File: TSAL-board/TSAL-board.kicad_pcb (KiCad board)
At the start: 2 copper layers, 82.5 x 65 mm, 75 parts, among them J1 BM02B-PASS-1-TF, J2 19427-0040, J3 BM02B-PASS-1-TF, J4 BM02B-PASS-1-TF, Q1 DMP3098LQ-7, Q2 2N7002K-AU, Q3 2N7002K-AU, Q4 2N7002K-AU, U1 TL431QDBVR, U2 TLP291(GB,SE, U3 TLC555QDRQ1

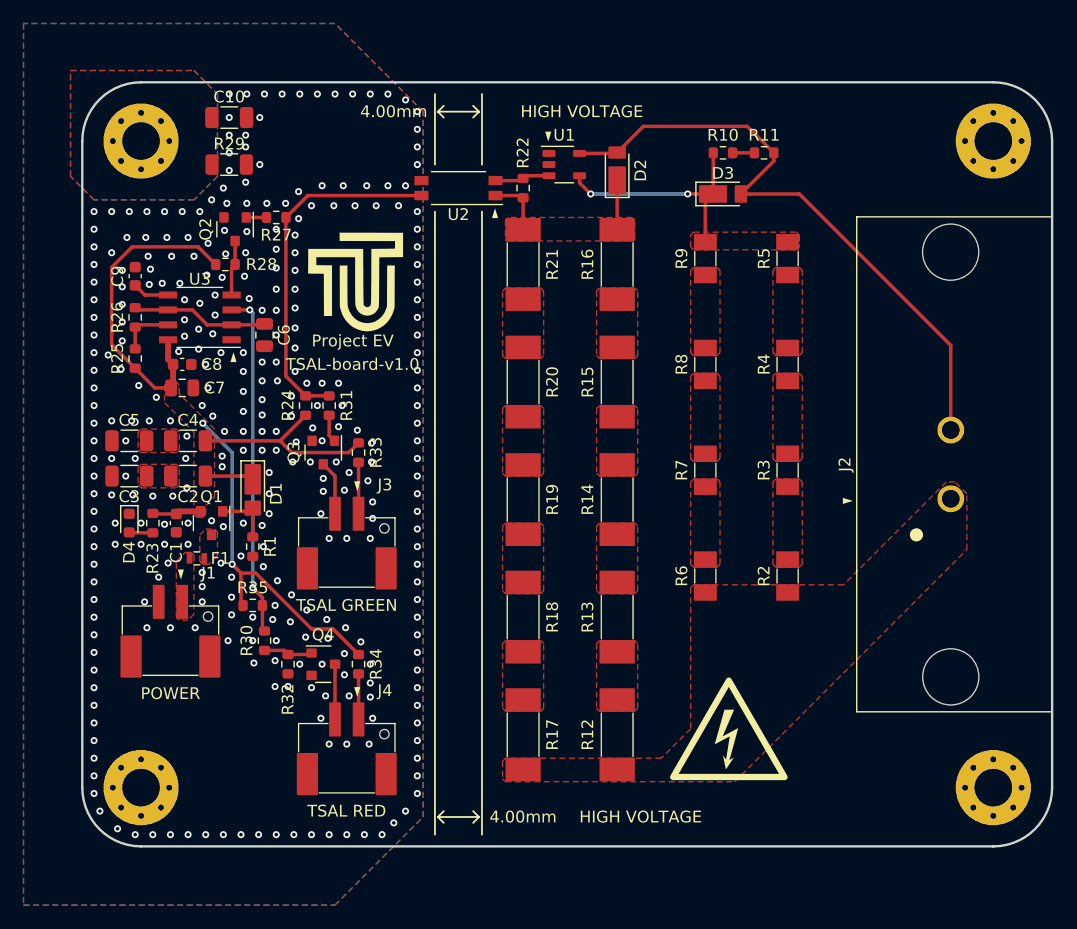
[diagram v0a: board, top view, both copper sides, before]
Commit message: 補償回路、シュミットトリガ回路追加
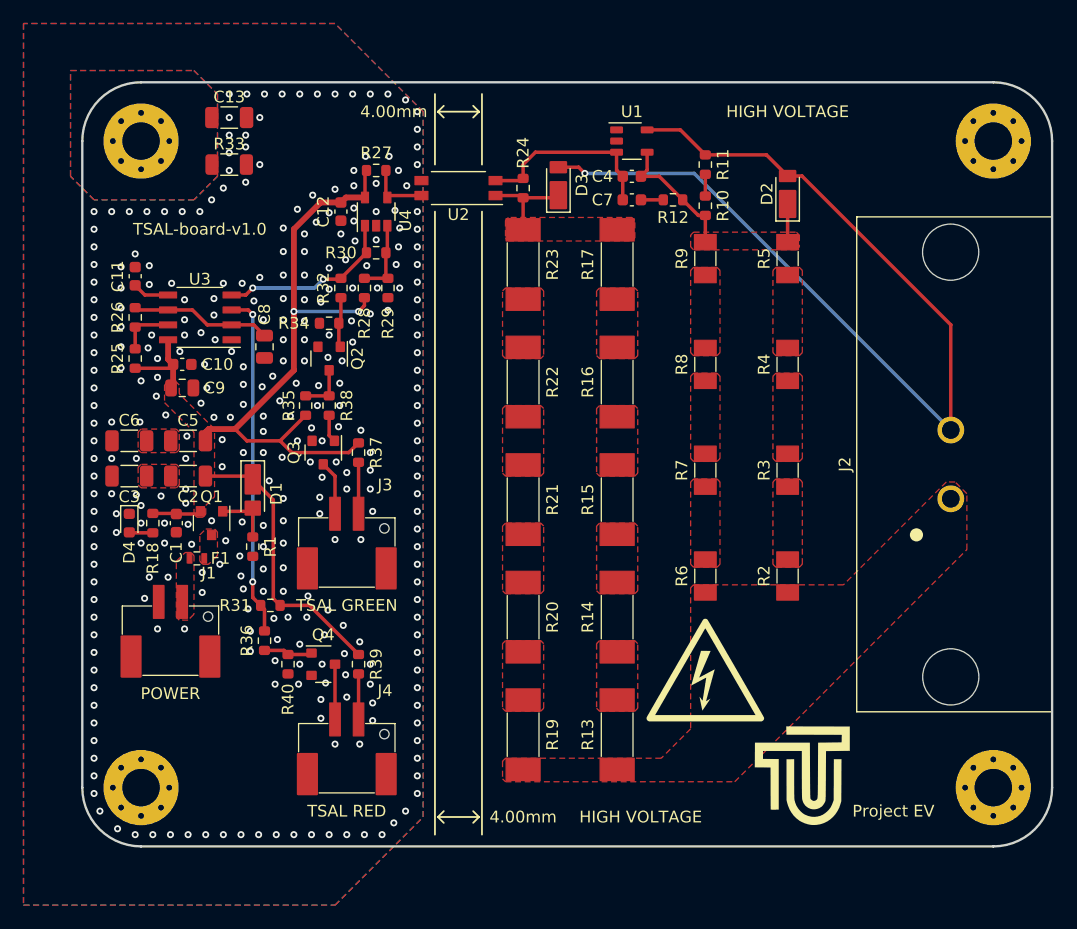
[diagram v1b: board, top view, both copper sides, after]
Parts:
- removed the R27 at (16.5, 11.5)
- removed REF** (x7): Identifier_1pin, ProjectEV:Identifier_1pin
- added C12: 0.1u, Capacitor_SMD:C_0603_1608Metric, F.Cu at (22.0, 11.0)
- added C4: 100p, Capacitor_SMD:C_0603_1608Metric, F.Cu at (46.8, 8.00)
- added C7: 10n, Capacitor_SMD:C_0603_1608Metric, F.Cu at (46.8, 10.0)
- added R12: 10k, Resistor_SMD:R_0603_1608Metric, F.Cu at (50.2, 10.0)
- added R29: 100k, Resistor_SMD:R_0603_1608Metric, F.Cu at (26.0, 17.5)
- added R30: 51k, Resistor_SMD:R_0603_1608Metric, F.Cu at (25.0, 14.5)
- added R32: 100, Resistor_SMD:R_0603_1608Metric, F.Cu at (22.0, 17.5)
- added R34: 1M, Resistor_SMD:R_0603_1608Metric, F.Cu at (21.0, 20.5)
- added R35: 100k, Resistor_SMD:R_0603_1608Metric, F.Cu at (19.0, 27.5)
- added U4: NCV20071SN2T1G, ProjectEV:Package_SOT-23-5_NCV20071SN2T1G, F.Cu at (25.0, 11.0)
- R11: value 3.9k -> 4.3k
- R27: renamed from R24; value 1M -> 10k
- moved G*** 56.6 mm to (61.0, 59.0)
- moved R27 20.9 mm to (25.0, 7.50), turned to 0 degrees
- moved Q2 13.6 mm to (21.0, 23.5)
- moved R28 12.0 mm to (24.0, 17.5), turned to 90 degrees
- moved U1 6.09 mm to (46.8, 5.00)
- moved D2 5.50 mm to (60.0, 9.50), turned to 90 degrees
- moved G*** 5.39 mm to (53.0, 50.0)
- moved D3 5.15 mm to (40.5, 8.75)
- moved R11 5.10 mm to (53.0, 7.00), turned to 90 degrees
- moved R10 4.74 mm to (53.0, 10.5), turned to 90 degrees
- moved R31 1.50 mm to (16.0, 44.5), turned to 180 degrees
- moved C8 1.00 mm to (15.5, 22.5)
- renumbered C8 to C10, C9 to C11, C10 to C13, C4 to C5, C5 to C6, C6 to C8, C7 to C9, D3 to D2, D2 to D3, R12 to R13, R13 to R14, R14 to R15, R15 to R16, R16 to R17, R23 to R18, R17 to R19, R18 to R20, R19 to R21, R20 to R22, R21 to R23, R22 to R24, R35 to R31, R29 to R33, R30 to R36, R33 to R37, R31 to R38, R34 to R39, R32 to R40
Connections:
- net Net-(C10-Pad1) renamed Earth
- Q2 pad 3: /~{RST} -> Net-(Q2-D)
- R28 pad 2: /~{RST} -> Net-(U4-+)
- R38 pad 1: /~{TS_ACTIVE} -> Net-(Q2-D)
- U3 pad 4: /~{RST} -> /TS_ACTIVE
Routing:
- net /TS-: track 53.5 -> 84.3 mm, vias 0 -> 1
- net /~{TS_ACTIVE}: track 30.2 -> 5.32 mm
- net /TS_ACTIVE: track 0.00 -> 15.3 mm, vias 0 -> 2
- net Net-(U1-K): track 4.72 -> 16.3 mm
- net +12V: track 82.6 -> 89.7 mm
- net Net-(U4-+): track 0.00 -> 6.60 mm
- net Net-(D2-K): track 20.2 -> 14.6 mm, vias 2 -> 0
- net /~{RST}: track 4.72 -> 0.00 mm
- net Net-(Q2-D): track 0.00 -> 4.18 mm
- net Net-(Q2-G): track 1.73 -> 4.30 mm
- net Net-(C7-Pad2): track 0.00 -> 1.90 mm
- net Net-(D3-K): track 9.35 -> 8.25 mm
- net GND: vias 322 -> 317

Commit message: 1ピン識別子追加
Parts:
- added REF**: Identifier_1pin, ProjectEV:Identifier_1pin, F.Cu at (8.50, 42.2)
- added REF**: Identifier_1pin, ProjectEV:Identifier_1pin, F.Cu at (35.2, 10.8)
- added REF**: Identifier_1pin, ProjectEV:Identifier_1pin, F.Cu at (44.2, 4.00)
- added REF**: Identifier_1pin, ProjectEV:Identifier_1pin, F.Cu at (23.0, 12.8)
- added REF**: Identifier_1pin, ProjectEV:Identifier_1pin, F.Cu at (13.2, 23.0)
- added REF**: Identifier_1pin, ProjectEV:Identifier_1pin, F.Cu at (23.5, 52.2)
- added REF**: Identifier_1pin, ProjectEV:Identifier_1pin, F.Cu at (65.2, 35.5)
- added REF**: Identifier_1pin, ProjectEV:Identifier_1pin, F.Cu at (23.5, 34.8)
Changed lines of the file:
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@@
     )
   )
+  (footprint "ProjectEV:Identifier_1pin" (layer "F.Cu")
+    (at 8.5 42.25)
+    (attr allow_missing_courtyard)
+    (fp_text reference "REF**" (at 0 -0.5 unlocked) (layer "F.SilkS") hide
+        (effects (font (size 1 1) (thickness 0.1)))
+    )
+    (fp_text value "Identifier_1pin" (at 0 1 unlocked) (layer "F.Fab")
+        (effects (font (size 1 1) (thickness 0.15)))
+    )
+    (fp_text user "▼" (at -0.375 0 unlocked) (layer "F.SilkS")
+        (effects (font (size 0.8 0.5) (thickness 0.125) bold) (justify left bottom))
+    )
+    (fp_text user "${REFERENCE}" (at 0 2.5 unlocked) (layer "F.Fab")
+        (effects (font (size 1 1) (thickness 0.15)))
+    )
+  )
   (footprint "Resistor_SMD:R_0603_1608Metric" (layer "F.Cu")
     (at 21 27.5 -90)
@@
       (net 17 "unconnected-(H4-Pad1)") (pinfunction "1") (pintype "input+no_connect") (zone_connect 2))
   )
+  (footprint "ProjectEV:Identifier_1pin" (layer "F.Cu")
+    (at 35.25 10.75 180)
+    (attr allow_missing_courtyard)
+    (fp_text reference "REF**" (at 0 -0.5 180 unlocked) (layer "F.SilkS") hide
+        (effects (font (size 1 1) (thickness 0.1)))
+    )
+    (fp_text value "Identifier_1pin" (at 0 1 180 unlocked) (layer "F.Fab")
+        (effects (font (size 1 1) (thickness 0.15)))
+    )
+    (fp_text user "▼" (at -0.375 0 180 unlocked) (layer "F.SilkS")
+        (effects (font (size 0.8 0.5) (thickness 0.125) bold) (justify left bottom))
+    )
+    (fp_text user "${REFERENCE}" (at 0 2.5 180 unlocked) (layer "F.Fab")
+        (effects (font (size 1 1) (thickness 0.15)))
+    )
+  )
   (footprint "Resistor_SMD:R_0603_1608Metric" (layer "F.Cu")
     (at 16 44.5 180)
@@
     )
   )
+  (footprint "ProjectEV:Identifier_1pin" (layer "F.Cu")
+    (at 44.25 4 90)
+    (attr allow_missing_courtyard)
+    (fp_text reference "REF**" (at 0 -0.5 90 unlocked) (layer "F.SilkS") hide
+        (effects (font (size 1 1) (thickness 0.1)))
+    )
+    (fp_text value "Identifier_1pin" (at 0 1 90 unlocked) (layer "F.Fab")
+        (effects (font (size 1 1) (thickness 0.15)))
+    )
+    (fp_text user "▼" (at -0.375 0 90 unlocked) (layer "F.SilkS")
+        (effects (font (size 0.8 0.5) (thickness 0.125) bold) (justify left bottom))
+    )
+    (fp_text user "${REFERENCE}" (at 0 2.5 90 unlocked) (layer "F.Fab")
+        (effects (font (size 1 1) (thickness 0.15)))
+    )
+  )
   (footprint "ProjectEV:R_TEConnectivity_3502" (layer "F.Cu")
     (at 37.5 45.5 90)
@@
       (net 10 "/TS-") (pinfunction "A") (pintype "passive") (thermal_bridge_angle 45))
   )
+  (footprint "ProjectEV:Identifier_1pin" (layer "F.Cu")
+    (at 23 12.75 90)
+    (attr allow_missing_courtyard)
+    (fp_text reference "REF**" (at 0 -0.5 90 unlocked) (layer "F.SilkS") hide
+        (effects (font (size 1 1) (thickness 0.1)))
+    )
+    (fp_text value "Identifier_1pin" (at 0 1 90 unlocked) (layer "F.Fab")
+        (effects (font (size 1 1) (thickness 0.15)))
+    )
+    (fp_text user "▼" (at -0.375 0 90 unlocked) (layer "F.SilkS")
+        (effects (font (size 0.8 0.5) (thickness 0.125) bold) (justify left bottom))
+    )
+    (fp_text user "${REFERENCE}" (at 0 2.5 90 unlocked) (layer "F.Fab")
+        (effects (font (size 1 1) (thickness 0.15)))
+    )
+  )
   (footprint "ProjectEV:R_TEConnectivity_3502" (layer "F.Cu")
     (at 45.5 35.5 90)
@@
     )
   )
+  (footprint "ProjectEV:Identifier_1pin" (layer "F.Cu")
+    (at 13.25 23 180)
+    (attr allow_missing_courtyard)
+    (fp_text reference "REF**" (at 0 -0.5 180 unlocked) (layer "F.SilkS") hide
+        (effects (font (size 1 1) (thickness 0.1)))
+    )
+    (fp_text value "Identifier_1pin" (at 0 1 180 unlocked) (layer "F.Fab")
+        (effects (font (size 1 1) (thickness 0.15)))
+    )
+    (fp_text user "▼" (at -0.375 0 180 unlocked) (layer "F.SilkS")
+        (effects (font (size 0.8 0.5) (thickness 0.125) bold) (justify left bottom))
+    )
+    (fp_text user "${REFERENCE}" (at 0 2.5 180 unlocked) (layer "F.Fab")
+        (effects (font (size 1 1) (thickness 0.15)))
+    )
+  )
   (footprint "ProjectEV:R_VishayDale_RCC1206-e3" (layer "F.Cu")
     (at 60 15 90)
@@
     )
   )
+  (footprint "ProjectEV:Identifier_1pin" (layer "F.Cu")
+    (at 23.5 52.25)
+    (attr allow_missing_courtyard)
+    (fp_text reference "REF**" (at 0 -0.5 unlocked) (layer "F.SilkS") hide
+        (effects (font (size 1 1) (thickness 0.1)))
+    )
+    (fp_text value "Identifier_1pin" (at 0 1 unlocked) (layer "F.Fab")
+        (effects (font (size 1 1) (thickness 0.15)))
+    )
+    (fp_text user "▼" (at -0.375 0 unlocked) (layer "F.SilkS")
+        (effects (font (size 0.8 0.5) (thickness 0.125) bold) (justify left bottom))
+    )
+    (fp_text user "${REFERENCE}" (at 0 2.5 unlocked) (layer "F.Fab")
+        (effects (font (size 1 1) (thickness 0.15)))
+    )
+  )
   (footprint "Resistor_SMD:R_0603_1608Metric" (layer "F.Cu")
     (at 25 7.5)
@@
     )
   )
+  (footprint "ProjectEV:Identifier_1pin" (layer "F.Cu")
+    (at 65.25 35.5 90)
+    (attr allow_missing_courtyard)
+    (fp_text reference "REF**" (at 0 -0.5 90 unlocked) (layer "F.SilkS") hide
+        (effects (font (size 1 1) (thickness 0.1)))
+    )
+    (fp_text value "Identifier_1pin" (at 0 1 90 unlocked) (layer "F.Fab")
+        (effects (font (size 1 1) (thickness 0.15)))
+    )
+    (fp_text user "▼" (at -0.375 0 90 unlocked) (layer "F.SilkS")
+        (effects (font (size 0.8 0.5) (thickness 0.125) bold) (justify left bottom))
+    )
+    (fp_text user "${REFERENCE}" (at 0 2.5 90 unlocked) (layer "F.Fab")
+        (effects (font (size 1 1) (thickness 0.15)))
+    )
+  )
   (footprint "Capacitor_SMD:C_0603_1608Metric" (layer "F.Cu")
     (at 4.5 16.5 -90)
@@
     )
   )
+  (footprint "ProjectEV:Identifier_1pin" (layer "F.Cu")
+    (at 23.5 34.75)
+    (attr allow_missing_courtyard)
+    (fp_text reference "REF**" (at 0 -0.5 unlocked) (layer "F.SilkS") hide
+        (effects (font (size 1 1) (thickness 0.1)))
+    )
+    (fp_text value "Identifier_1pin" (at 0 1 unlocked) (layer "F.Fab")
+        (effects (font (size 1 1) (thickness 0.15)))
+    )
+    (fp_text user "▼" (at -0.375 0 unlocked) (layer "F.SilkS")
+        (effects (font (size 0.8 0.5) (thickness 0.125) bold) (justify left bottom))
+    )
+    (fp_text user "${REFERENCE}" (at 0 2.5 unlocked) (layer "F.Fab")
+        (effects (font (size 1 1) (thickness 0.15)))
+    )
+  )
